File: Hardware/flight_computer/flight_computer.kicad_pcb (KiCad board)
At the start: 4 copper layers, 80 x 100 mm, 114 parts, among them J1 Micro_USB, J2 MicroSD_molex, J3 rpi_zero_w, J4 JST_8_RA, J5 JST_GH_6_RA, J6 JST_GH_4_RA, J7 JST_GH_5_RA, J8 Conn_02x03, J9 Conn_02x03, Q2 PMOS_20V_.76A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

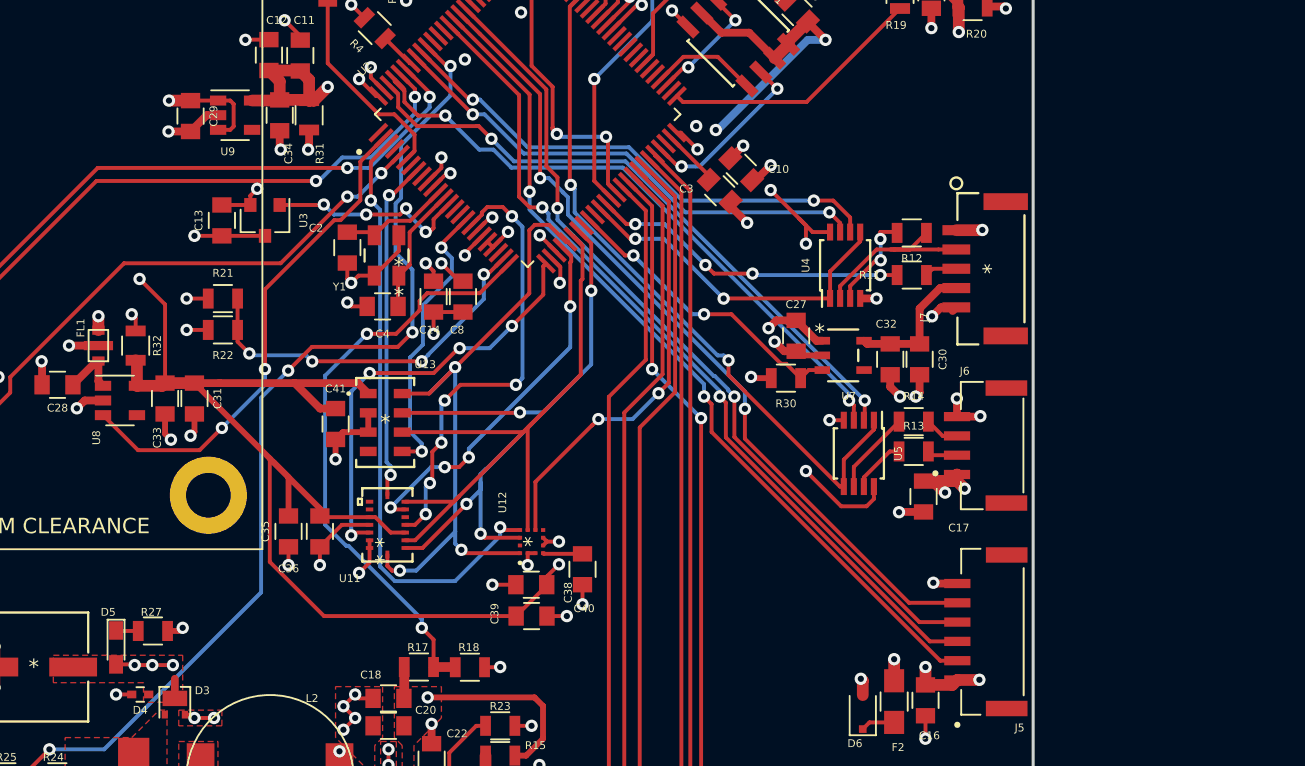
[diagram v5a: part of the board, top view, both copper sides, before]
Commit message: updated LEDs
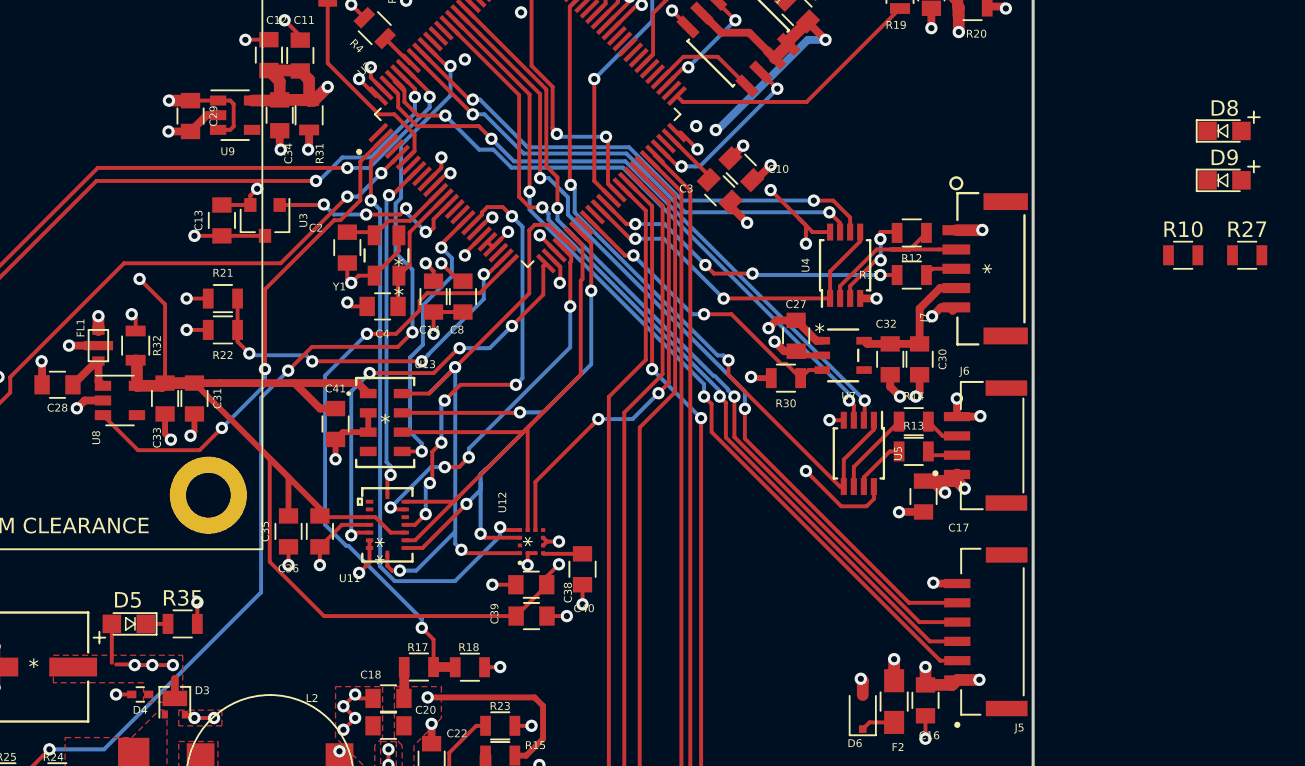
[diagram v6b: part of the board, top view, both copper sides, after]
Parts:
- removed G***: LOGO, drone_footprints:osprey_bitmap
- added D8: LED_0805_Green, drone_footprints:LED_0805, F.Cu at (171.9, 108.5)
- added D9: LED_0805_Red, drone_footprints:LED_0805, F.Cu at (171.9, 111.7)
- added R10: R_51.1, Resistors_SMD:R_0805, F.Cu at (169.2, 116.6)
- added R35: R_120, Resistors_SMD:R_0805, F.Cu at (104.4, 140.5)
- D5: value LED_GREEN -> LED_0805_Green; footprint LEDs:LED_0603_HandSoldering -> drone_footprints:LED_0805
- R27: value R_220 -> R_51.1
- moved R27 75.0 mm to (173.4, 116.6)
- moved D5 1.73 mm to (100.9, 140.5), turned to 180 degrees
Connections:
- R27 pad 1: Net-(D5-Pad1) -> Net-(D9-Pad1)
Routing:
- net /VDD_5V_IN: track 21.6 -> 24.2 mm

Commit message: added new bom, bad gerber files, and messed with layout
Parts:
- moved R10 92.1 mm to (93.5, 64.3), turned to 90 degrees
- moved D8 88.5 mm to (93.5, 67.6), turned to 270 degrees
- moved R27 88.2 mm to (102.4, 64.3), turned to 90 degrees
- moved D9 82.4 mm to (102.4, 67.6), turned to 270 degrees
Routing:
- net /GPS_USART6_TX: track 31.0 -> 32.8 mm
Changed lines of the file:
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@@
     (thickness 1.6)
     (drawings 13)
-    (tracks 1470)
+    (tracks 1476)
     (zones 0)
     (modules 117)
@@
   (layers
     (0 F.Cu signal)
-    (1 In1.Cu power)
-    (2 In2.Cu power)
+    (1 In1.Cu power hide)
+    (2 In2.Cu power hide)
     (31 B.Cu signal)
     (32 B.Adhes user hide)
@@
       (outputformat 1)
       (mirror false)
-      (drillshape 1)
+      (drillshape 0)
       (scaleselection 1)
-      (outputdirectory ""))
+      (outputdirectory "../../gerber/"))
   )
   (net 0 "")
@@
   )
   (module Resistors_SMD:R_0805 (layer F.Cu)
-    (at 169.222001 116.573501)
+    (at 93.472 64.262 90)
     (descr "Resistor SMD 0805, reflow soldering, Vishay (see dcrcw.pdf)")
     (tags "resistor 0805")
     (attr smd)
-    (fp_text reference R10 (at 0 -1.65) (layer F.SilkS)
+    (fp_text reference R10 (at 0 -1.65 90) (layer F.SilkS)
       (effects (font (size 1 1) (thickness 0.15)))
     )
-    (fp_text value R_51.1 (at 0 1.75) (layer F.Fab)
+    (fp_text value R_51.1 (at 0 1.75 90) (layer F.Fab)
       (effects (font (size 1 1) (thickness 0.15)))
     )
@@
     (fp_line (start 1 0.62) (end -1 0.62) (layer F.Fab) (width 0.1))
     (fp_line (start -1 0.62) (end -1 -0.62) (layer F.Fab) (width 0.1))
-    (fp_text user %R (at 0 0) (layer F.Fab)
+    (fp_text user %R (at 0 0 90) (layer F.Fab)
       (effects (font (size 0.5 0.5) (thickness 0.075)))
     )
-    (pad 2 smd rect (at 0.95 0) (size 0.7 1.3) (layers F.Cu F.Paste F.Mask)
+    (pad 2 smd rect (at 0.95 0 90) (size 0.7 1.3) (layers F.Cu F.Paste F.Mask)
       (net 1 GND))
-    (pad 1 smd rect (at -0.95 0) (size 0.7 1.3) (layers F.Cu F.Paste F.Mask)
+    (pad 1 smd rect (at -0.95 0 90) (size 0.7 1.3) (layers F.Cu F.Paste F.Mask)
       (net 181 "Net-(D8-Pad1)"))
     (model ${KISYS3DMOD}/Resistors_SMD.3dshapes/R_0805.wrl
@@
   )
   (module Resistors_SMD:R_0805 (layer F.Cu)
-    (at 173.372001 116.573501)
+    (at 102.362 64.262 90)
     (descr "Resistor SMD 0805, reflow soldering, Vishay (see dcrcw.pdf)")
     (tags "resistor 0805")
     (attr smd)
-    (fp_text reference R27 (at 0 -1.65) (layer F.SilkS)
+    (fp_text reference R27 (at 0 -1.65 90) (layer F.SilkS)
       (effects (font (size 1 1) (thickness 0.15)))
     )
-    (fp_text value R_51.1 (at 0 1.75) (layer F.Fab)
+    (fp_text value R_51.1 (at 0 1.75 90) (layer F.Fab)
       (effects (font (size 1 1) (thickness 0.15)))
     )
@@
     (fp_line (start 1 0.62) (end -1 0.62) (layer F.Fab) (width 0.1))
     (fp_line (start -1 0.62) (end -1 -0.62) (layer F.Fab) (width 0.1))
-    (fp_text user %R (at 0 0) (layer F.Fab)
+    (fp_text user %R (at 0 0 90) (layer F.Fab)
       (effects (font (size 0.5 0.5) (thickness 0.075)))
     )
-    (pad 2 smd rect (at 0.95 0) (size 0.7 1.3) (layers F.Cu F.Paste F.Mask)
+    (pad 2 smd rect (at 0.95 0 90) (size 0.7 1.3) (layers F.Cu F.Paste F.Mask)
       (net 1 GND))
-    (pad 1 smd rect (at -0.95 0) (size 0.7 1.3) (layers F.Cu F.Paste F.Mask)
+    (pad 1 smd rect (at -0.95 0 90) (size 0.7 1.3) (layers F.Cu F.Paste F.Mask)
       (net 182 "Net-(D9-Pad1)"))
     (model ${KISYS3DMOD}/Resistors_SMD.3dshapes/R_0805.wrl
@@
   )
   (module drone_footprints:LED_0805 (layer F.Cu)
-    (at 171.901001 108.518001)
+    (at 93.472 67.564 270)
     (descr "LED 0805 smd package")
     (tags "LED led 0805 SMD smd SMT smt smdled SMDLED smtled SMTLED")
     (attr smd)
-    (fp_text reference D8 (at 0 -1.45) (layer F.SilkS)
+    (fp_text reference D8 (at 0 -1.45 90) (layer F.SilkS)
       (effects (font (size 1 1) (thickness 0.15)))
     )
-    (fp_text value LED_0805_Green (at 0 1.55) (layer F.Fab)
+    (fp_text value LED_0805_Green (at 0 1.55 90) (layer F.Fab)
       (effects (font (size 1 1) (thickness 0.15)))
     )
@@
     (fp_line (start 1.524 -0.889) (end 2.286 -0.889) (layer F.SilkS) (width 0.12))
     (fp_line (start 1.905 -1.143) (end 1.905 -1.27) (layer F.SilkS) (width 0.12))
-    (pad 1 smd rect (at -1.1 0 180) (size 1.2 1.2) (layers F.Cu F.Paste F.Mask)
+    (pad 1 smd rect (at -1.1 0 90) (size 1.2 1.2) (layers F.Cu F.Paste F.Mask)
       (net 181 "Net-(D8-Pad1)"))
-    (pad 2 smd rect (at 1.1 0 180) (size 1.2 1.2) (layers F.Cu F.Paste F.Mask)
+    (pad 2 smd rect (at 1.1 0 90) (size 1.2 1.2) (layers F.Cu F.Paste F.Mask)
       (net 171 /DEBUG_LED_1))
     (model ${KISYS3DMOD}/LEDs.3dshapes/LED_0805.wrl
@@
   )
   (module drone_footprints:LED_0805 (layer F.Cu)
-    (at 171.901001 111.718001)
+    (at 102.362 67.564 270)
     (descr "LED 0805 smd package")
     (tags "LED led 0805 SMD smd SMT smt smdled SMDLED smtled SMTLED")
     (attr smd)
-    (fp_text reference D9 (at 0 -1.45) (layer F.SilkS)
+    (fp_text reference D9 (at 0 -1.45 90) (layer F.SilkS)
       (effects (font (size 1 1) (thickness 0.15)))
     )
-    (fp_text value LED_0805_Red (at 0 1.55) (layer F.Fab)
+    (fp_text value LED_0805_Red (at 0 1.55 90) (layer F.Fab)
       (effects (font (size 1 1) (thickness 0.15)))
     )
@@
     (fp_line (start -1.95 0.85) (end -1.95 -0.85) (layer F.CrtYd) (width 0.05))
     (fp_line (start -1.95 -0.85) (end 1.95 -0.85) (layer F.CrtYd) (width 0.05))
-    (pad 2 smd rect (at 1.1 0 180) (size 1.2 1.2) (layers F.Cu F.Paste F.Mask)
+    (pad 2 smd rect (at 1.1 0 90) (size 1.2 1.2) (layers F.Cu F.Paste F.Mask)
       (net 172 /DEBUG_LED_2))
-    (pad 1 smd rect (at -1.1 0 180) (size 1.2 1.2) (layers F.Cu F.Paste F.Mask)
+    (pad 1 smd rect (at -1.1 0 90) (size 1.2 1.2) (layers F.Cu F.Paste F.Mask)
       (net 182 "Net-(D9-Pad1)"))
     (model ${KISYS3DMOD}/LEDs.3dshapes/LED_0805.wrl
@@
   (segment (start 133.061573 116.586) (end 130.762367 114.286794) (width 0.254) (layer F.Cu) (net 103))
   (segment (start 133.604 116.586) (end 133.061573 116.586) (width 0.254) (layer F.Cu) (net 103))
-  (via (at 133.35 99.822) (size 0.8) (drill 0.4) (layers F.Cu B.Cu) (net 104))
-  (segment (start 131.823027 101.657867) (end 133.35 100.130894) (width 0.254) (layer F.Cu) (net 104))
-  (segment (start 133.35 100.130894) (end 133.35 99.822) (width 0.254) (layer F.Cu) (net 104))
   (via (at 141.224 77.216) (size 0.8) (drill 0.4) (layers F.Cu B.Cu) (net 104))
   (segment (start 141.224 77.216) (end 141.224 75.626) (width 0.254) (layer F.Cu) (net 104))
-  (segment (start 140.97 92.202) (end 133.35 99.822) (width 0.254) (layer B.Cu) (net 104))
-  (segment (start 141.224 77.216) (end 140.97 77.47) (width 0.254) (layer B.Cu) (net 104))
-  (segment (start 140.97 77.47) (end 140.97 92.202) (width 0.254) (layer B.Cu) (net 104))
+  (segment (start 131.936997 101.657867) (end 133.858 99.736864) (width 0.254) (layer F.Cu) (net 104))
+  (segment (start 131.823027 101.657867) (end 131.936997 101.657867) (width 0.254) (layer F.Cu) (net 104))
+  (via (at 137.335917 95.9979) (size 0.8) (drill 0.4) (layers F.Cu B.Cu) (net 104))
+  (segment (start 133.858 99.736864) (end 133.858 99.475817) (width 0.254) (layer F.Cu) (net 104))
+  (segment (start 133.858 99.475817) (end 137.335917 95.9979) (width 0.254) (layer F.Cu) (net 104))
+  (segment (start 140.97 77.47) (end 141.224 77.216) (width 0.254) (layer B.Cu) (net 104))
+  (segment (start 140.97 92.3544) (end 140.97 77.47) (width 0.254) (layer B.Cu) (net 104))
+  (segment (start 137.735916 95.588484) (end 140.97 92.3544) (width 0.254) (layer B.Cu) (net 104))
+  (segment (start 137.335917 95.9979) (end 137.735916 95.597901) (width 0.254) (layer B.Cu) (net 104))
+  (segment (start 137.735916 95.597901) (end 137.735916 95.588484) (width 0.254) (layer B.Cu) (net 104))
   (segment (start 145.43684 71.87802) (end 146.04084 71.87802) (width 0.254) (layer F.Cu) (net 105))
   (segment (start 142.46798 71.87802) (end 145.43684 71.87802) (width 0.254) (layer F.Cu) (net 105))
   (segment (start 141.224 73.122) (end 142.46798 71.87802) (width 0.254) (layer F.Cu) (net 105))
   (segment (start 141.224 73.726) (end 141.224 73.122) (width 0.254) (layer F.Cu) (net 105))
-  (via (at 134.142446 100.350297) (size 0.8) (drill 0.4) (layers F.Cu B.Cu) (net 106))
-  (segment (start 132.17658 102.01142) (end 133.837703 100.350297) (width 0.254) (layer F.Cu) (net 106))
-  (segment (start 133.837703 100.350297) (end 134.142446 100.350297) (width 0.254) (layer F.Cu) (net 106))
   (via (at 143.002 77.216) (size 0.8) (drill 0.4) (layers F.Cu B.Cu) (net 106))
   (segment (start 143.002 75.626) (end 143.002 77.216) (width 0.254) (layer F.Cu) (net 106))
-  (segment (start 134.142446 99.604304) (end 134.142446 100.350297) (width 0.254) (layer B.Cu) (net 106))
-  (segment (start 141.376409 92.370341) (end 134.142446 99.604304) (width 0.254) (layer B.Cu) (net 106))
-  (segment (start 143.002 77.216) (end 141.37641 78.84159) (width 0.254) (layer B.Cu) (net 106))
-  (segment (start 141.37641 78.84159) (end 141.376409 92.370341) (width 0.254) (layer B.Cu) (net 106))
+  (via (at 141.3764 95.9979) (size 0.8) (drill 0.4) (layers F.Cu B.Cu) (net 106))
+  (segment (start 139.73925 97.63505) (end 141.3764 95.9979) (width 0.254) (layer F.Cu) (net 106))
+  (segment (start 132.17658 102.01142) (end 136.55295 97.63505) (width 0.254) (layer F.Cu) (net 106))
+  (segment (start 136.55295 97.63505) (end 139.73925 97.63505) (width 0.254) (layer F.Cu) (net 106))
+  (segment (start 141.37641 78.84159) (end 143.002 77.216) (width 0.254) (layer B.Cu) (net 106))
+  (segment (start 141.401185 92.760185) (end 141.376409 92.735409) (width 0.254) (layer B.Cu) (net 106))
+  (segment (start 141.376409 92.735409) (end 141.37641 78.84159) (width 0.254) (layer B.Cu) (net 106))
+  (segment (start 141.3764 95.9979) (end 141.401185 95.973115) (width 0.254) (layer B.Cu) (net 106))
+  (segment (start 141.401185 95.973115) (end 141.401185 92.760185) (width 0.254) (layer B.Cu) (net 106))
   (segment (start 143.906 73.726) (end 144.226 73.406) (width 0.254) (layer F.Cu) (net 107))
   (segment (start 143.002 73.726) (end 143.906 73.726) (width 0.254) (layer F.Cu) (net 107))

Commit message: Traces out debug LEDs
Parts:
- added G***: LOGO, drone_footprints:osprey_bitmap, B.Cu at (121.9, 104.9)
- moved R10 76.1 mm to (155.4, 108.5), turned to 0 degrees
- moved D8 71.2 mm to (151.8, 108.5), turned to 180 degrees
- moved R27 67.2 mm to (155.4, 105.4), turned to 0 degrees
- moved D9 62.3 mm to (151.8, 105.4), turned to 180 degrees
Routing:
- net /DEBUG_LED_1: track 0.00 -> 23.8 mm, vias 0 -> 2
- net /DEBUG_LED_2: track 0.00 -> 23.1 mm, vias 0 -> 2
- net GND: track 238.6 -> 241.1 mm, vias 107 -> 109
- net Net-(D9-Pad1): track 0.00 -> 1.59 mm
- net Net-(D8-Pad1): track 0.00 -> 1.59 mm
